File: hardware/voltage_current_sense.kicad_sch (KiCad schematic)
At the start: 0 parts

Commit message: sensing schematics
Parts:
- added C10, C9: 0.22uF, symbol Device:C
- added C11, C12, C15, C16: 0.1uF, symbol Device:C
- added C13: 1uF, symbol Device:C
- added C14: 4.7nF, symbol Device:C
- added C17: 1nF, symbol Device:C
- added R23, R24: 0.82k, symbol Device:R
- added R25, R26, R29, R33, R35: 10k, symbol Device:R
- added R27: 100, symbol Device:R
- added R28, R34: 910k, symbol Device:R
- added R30: 50k, symbol Device:R
- added R31: 360, symbol Device:R
- added R32: 2.2k, symbol Device:R
- added U10: NME0505SC, SIP04_NME_11P53X6P1_MUR, symbol NME0505SC:NME0505SC
- added U6: INA126U/2K5, D0008A_N, symbol INA126:INA126U_2K5
- added U7: (no value), symbol discharger:HASS_300S
- added U8: LTC6992CS6-2-TRMPBF, 05-08-1636_ADI, symbol LTC6992CS6_2_TRMPBF:LTC6992CS6-2-TRMPBF
- added U9: 6N137, Package_DIP:DIP-8_W7.62mm, symbol Isolator:6N137
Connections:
- new net: C14.1, C9.1, R23.2, U6.2 (-IN)
- new net: R24.1, U7.1 (Vref)
- new net: R23.1, U7.2 (Output)
- new net: R28.1, R29.2, R34.1, U8.1 (MOD)
- new net: R30.2, U8.3 (SET)
- new net: C11.1, U8.4 (DIV)
- new net: R31.2, U8.6 (OUT)
- new net: C17.1, R27.1
- new net: R33.2, U9.7 (EN)
- new net: R31.1, U9.2 (A)
- new net: R32.2, U9.6 (VO)
- new net: C10.1, C14.2, R24.2, U6.3 (+IN)
- new net: R27.2, U6.6 (VOUT)
- new net: R35.1, U6.1 (RG)
- new net: C13.1, R25.1, R26.2, U6.5 (REF)
- new net: R35.2, U6.8 (RG)
- new net: R28.2, R34.2
- new net +3.3V: R32.1
- new net +5V: C15.1, C16.1, R25.2, U10.2 (+VIN), U6.7 (V+), U7.4 (+5V)
- new net +5V_isolated: C11.2, C12.1, U10.4 (+VOUT), U8.5 (V+), U9.8 (VCC)
- new net GND: C10.2, C12.2, C13.2, C15.2, C16.2, C17.2, C9.2, R26.1, R30.1, R33.1, U10.1 (-VIN), U6.4 (V-), U7.3 (GND), U9.3 (C), U9.5 (GND)
- new net HV_GND: R29.1, U10.3 (-VOUT), U8.2 (GND)
- no-connect marks 0 -> 2
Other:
- note added: "Current Sensing"
- note added: "Voltage Sensing"

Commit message: pushing all changes
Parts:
- added C18: 1uF, symbol Device:C
- added C19: 10uF, symbol Device:C
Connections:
- net +5V_isolated: now also C18.1, C19.1
- net GND: no longer R30.1
- net HV_GND: now also R30.1, C18.2, C19.2
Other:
- moved on the sheet: R32, U10

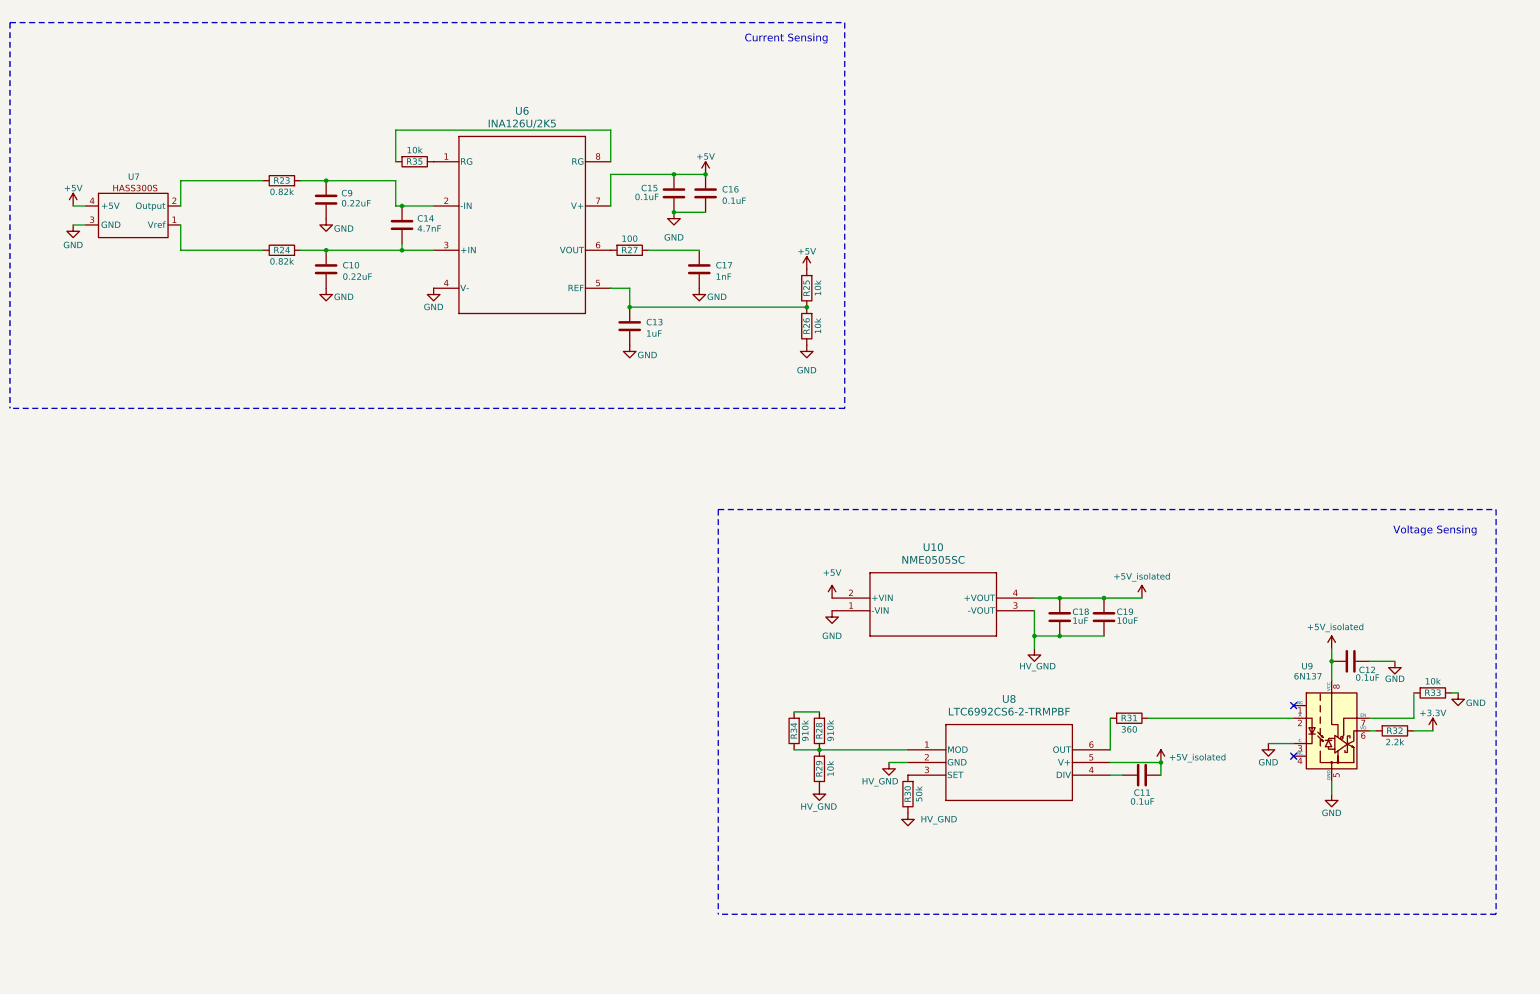
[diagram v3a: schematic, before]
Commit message: R0.0.3 Correct Voltage measurement frequency and divider
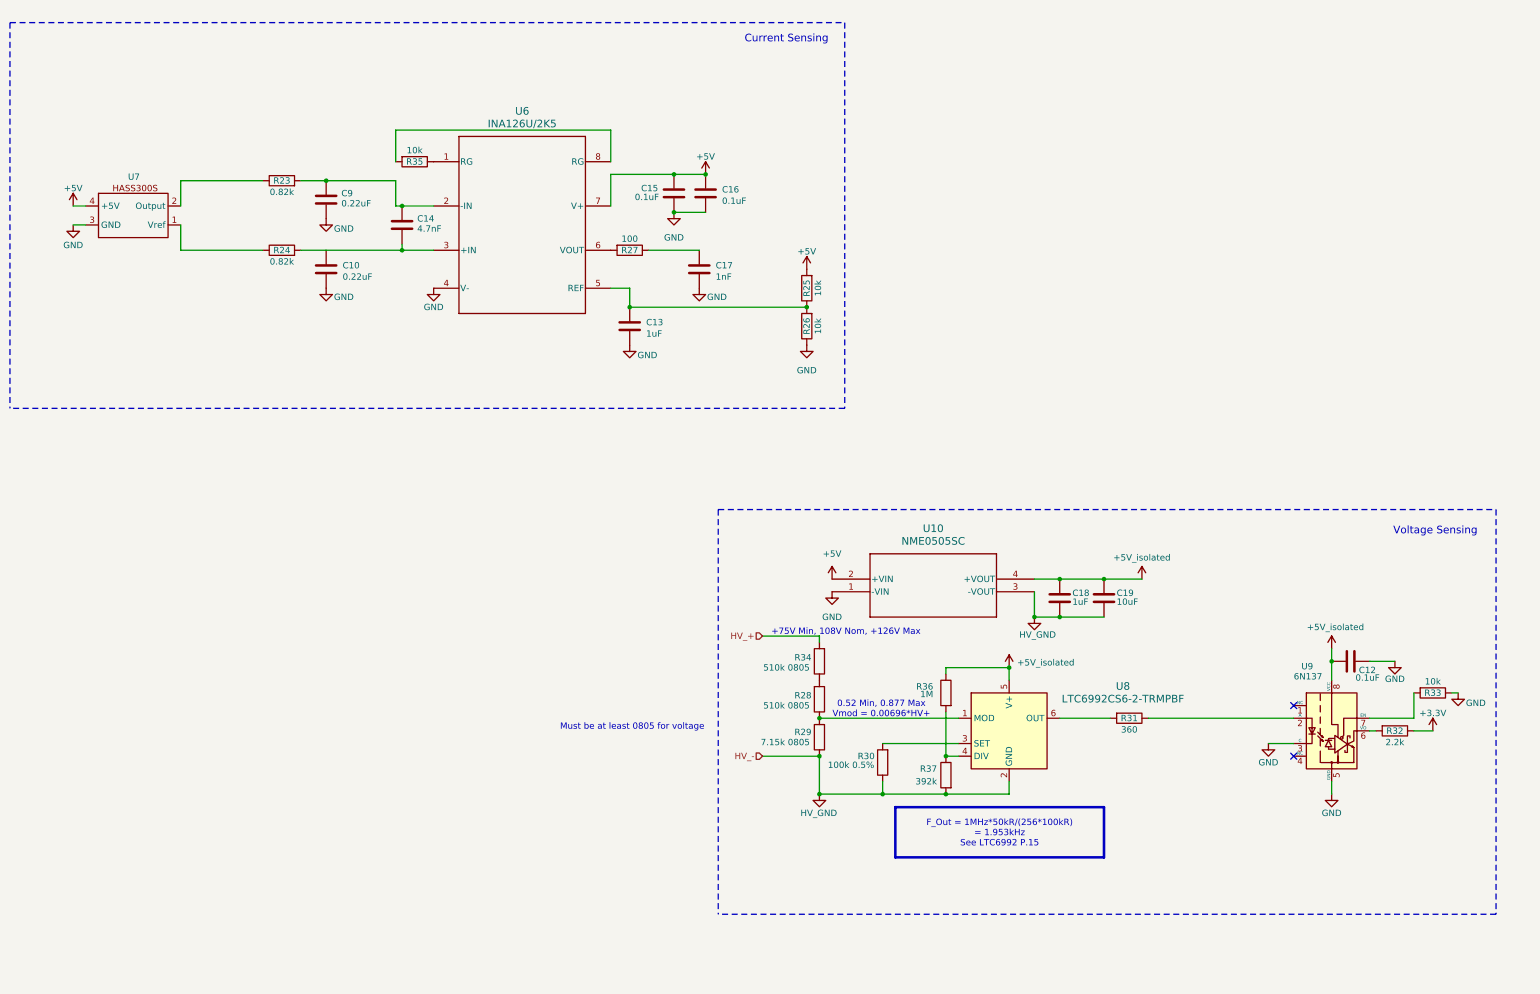
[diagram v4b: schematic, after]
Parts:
- removed C11: 0.1uF, symbol Device:C
- added R36: 1M, symbol Device:R
- added R37: 392k, symbol Device:R
- R28, R34: value 910k -> 510k 0805
- R29: value 10k -> 7.15k 0805
- R30: value 50k -> 100k 0.5%
- U8: footprint 05-08-1636_ADI -> Package_TO_SOT_SMD:TSOT-23-6; symbol LTC6992CS6_2_TRMPBF:LTC6992CS6-2-TRMPBF -> discharger:LTC6992CS6-2-TRMPBF; Digi PN (none) -> 505-LTC6992CS6-2#TRMPBFCT-ND; Digi URL (none) -> https://www.digikey.com/en/products/detail/analog-devices-i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; MFG (none) -> Analog Devices Inc.; MFG PN (none) -> LTC6992CS6-2-TRMPBF
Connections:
- net +5V_isolated: now also R36.1
- net HV_GND: now also R37.2
- net at R28.1, R29.2, U8.1 (MOD): no longer R34.1
- net at U8.4 (DIV): now also R36.2, R37.1
- net at R28.2: now also R34.1; no longer R34.2
- new net HV_+: R34.2
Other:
- note added: "+75V Min, 108V Nom, +126V Max"
- note added: "0.52 Min, 0.877 Max Vmod = 0.00696*HV+"
- note added: "Must be at least 0805 for voltage"
- title: [BOARD NAME] -> Discharger Main Board
- moved on the sheet: C18, C19, R28, R29, R30, R34, U10

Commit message: new sensor changes, need to still add low pass for voltage
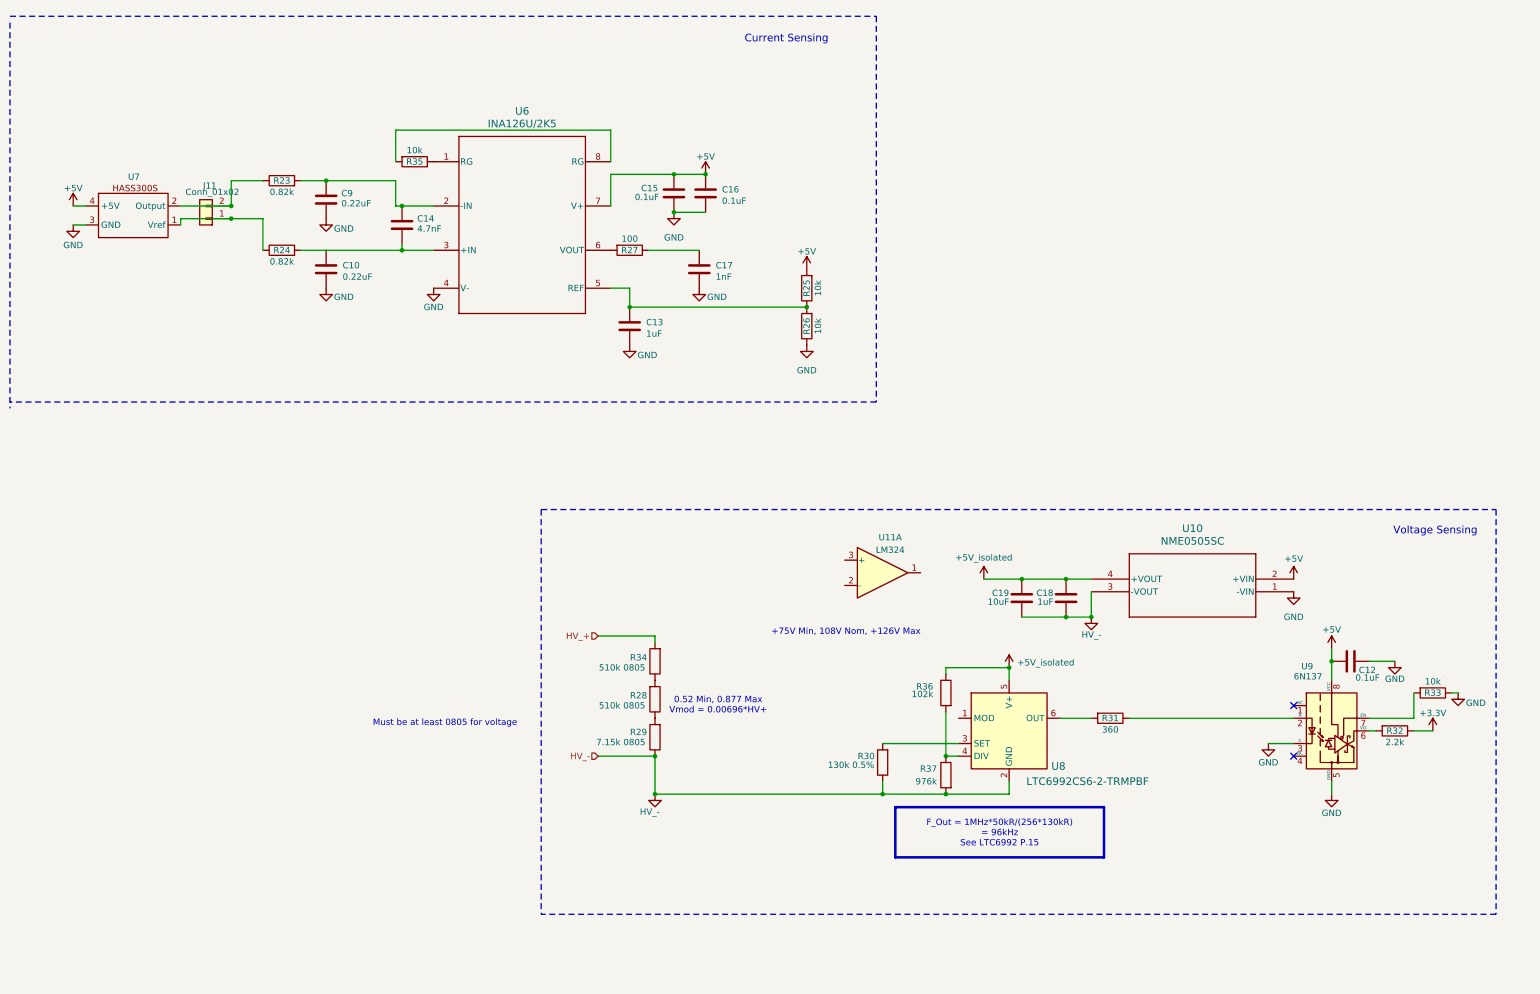
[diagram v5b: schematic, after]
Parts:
- added J11: Conn_01x02, symbol Connector_Generic:Conn_01x02
- added U11: LM324, symbol Amplifier_Operational:LM324
- R30: value 100k 0.5% -> 130k 0.5%
- R36: value 1M -> 102k
- R37: value 392k -> 976k
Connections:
- net +5V: now also C12.1, U9.8 (VCC)
- net +5V_isolated: no longer C12.1, U9.8 (VCC)
- net at R24.1, U7.1 (Vref): now also J11.1 (Pin_1)
- net at R23.1, U7.2 (Output): now also J11.2 (Pin_2)
- net at R28.1, R29.2: no longer U8.1 (MOD)
- net HV_GND renamed HV_-
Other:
- moved on the sheet: C18, C19, R28, R29, R31, R34, U10

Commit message: adding connectors
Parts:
- removed J11: Conn_01x02, symbol Connector_Generic:Conn_01x02
- added C11: 20.5nF, symbol Device:C
- added C20: 10nF, symbol Device:C
- added R38: 13k, symbol Device:R
- added R39: 9.53k, symbol Device:R
- added unit 5 of U11
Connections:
- net +5V: now also U11.4 (V+)
- net GND: no longer U9.3 (C)
- net HV_-: now also U9.3 (C), C20.1, U11.11 (V-)
- net CurrentSens_Vref: now reaches R24.1, U7.1 (Vref)
- net CurrentSens_Out: now reaches R23.1, U7.2 (Output)
- net at U8.1 (MOD): now also U11.1, U11.2 (-), C11.2
- net Current_Out: now reaches C13.1, R25.1, R26.2, U6.5 (REF)
- net at R28.1, R29.2: now also R39.1
- net at U11.3 (+): now also C20.2, R38.2
- new net: C11.1, R38.1, R39.2
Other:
- moved on the sheet: C12, C18, C19, R28, R29, R30, R31, R32, R33, R34, R36, R37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

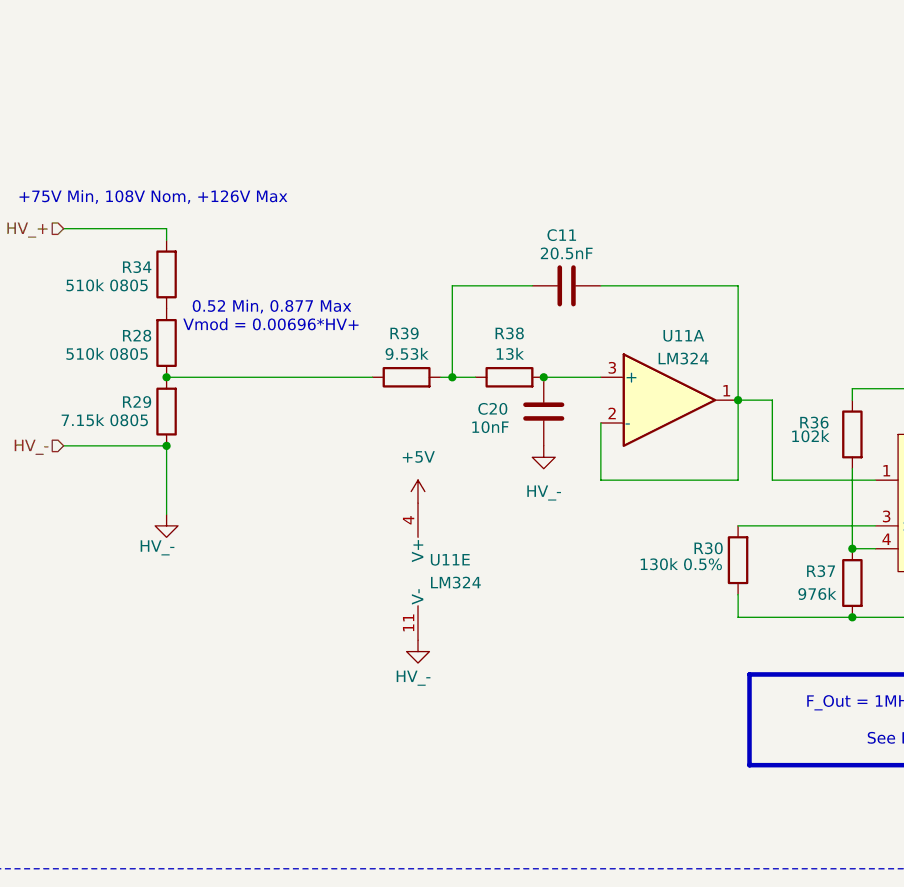
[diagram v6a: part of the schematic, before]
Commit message: chebyshev filter for voltage sense 2.0
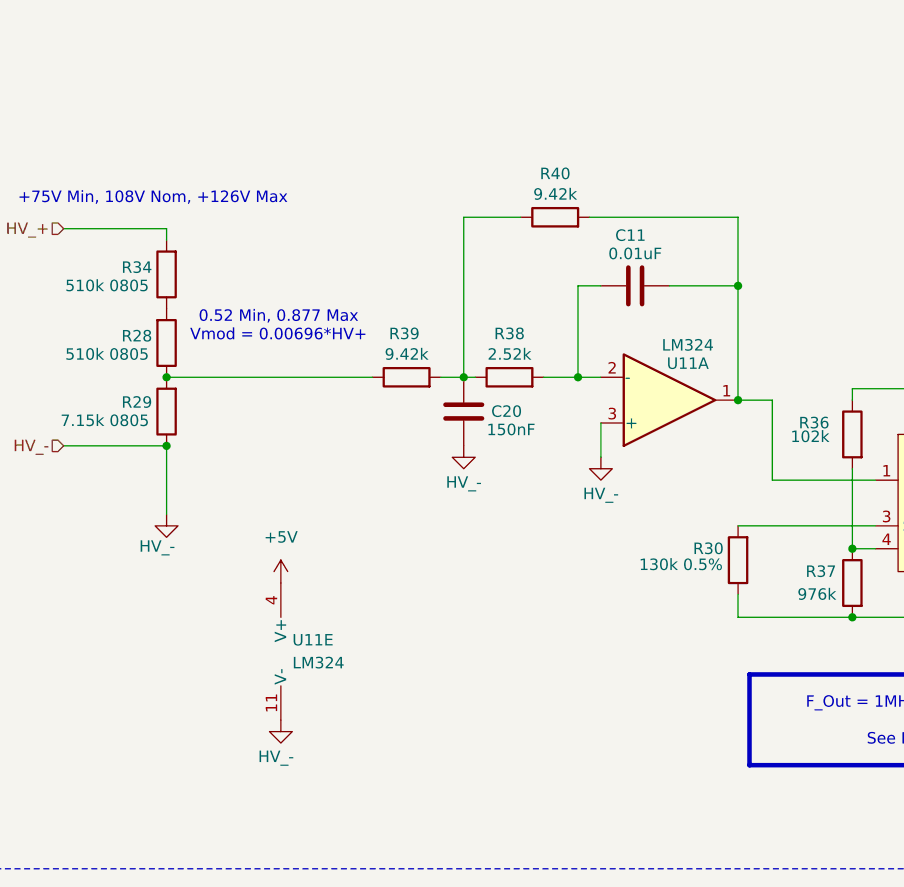
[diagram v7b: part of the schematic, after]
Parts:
- added R40: 9.42k, symbol Device:R
- C11: value 20.5nF -> 0.01uF
- C20: value 10nF -> 150nF
- R38: value 13k -> 2.52k
- R39: value 9.53k -> 9.42k
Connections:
- net HV_-: now also U11.3 (+)
- net at C11.2, U11.1, U8.1 (MOD): now also R40.2; no longer U11.2 (-)
- net at R38.1, R39.2: now also C20.2, R40.1; no longer C11.1
- new net: C11.1, R38.2, U11.2 (-)
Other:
- moved on the sheet: U11E

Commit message: Pin assignment first draft
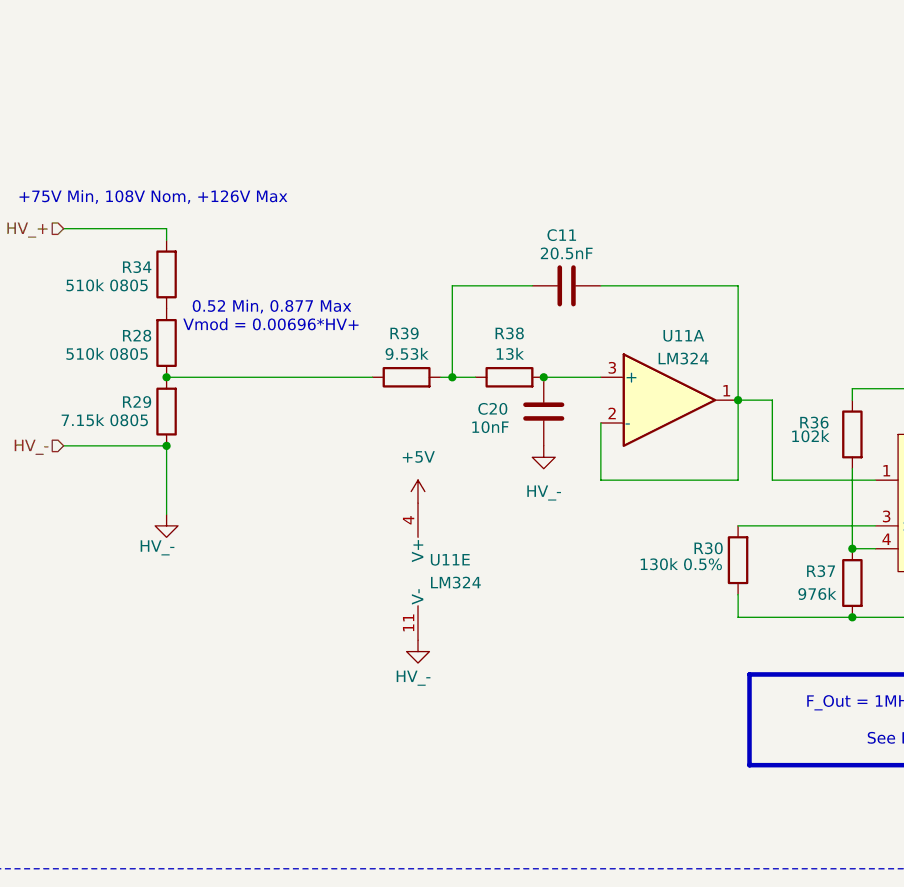
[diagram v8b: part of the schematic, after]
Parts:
- removed R40: 9.42k, symbol Device:R
- C11: value 0.01uF -> 20.5nF
- C20: value 150nF -> 10nF
- R38: value 2.52k -> 13k
- R39: value 9.42k -> 9.53k
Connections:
- net HV_-: no longer U11.3 (+)
- net at C11.2, U11.1, U8.1 (MOD): now also U11.2 (-)
- net at R38.1, R39.2: now also C11.1; no longer C20.2
- new net: C20.2, R38.2, U11.3 (+)
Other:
- moved on the sheet: U11E
